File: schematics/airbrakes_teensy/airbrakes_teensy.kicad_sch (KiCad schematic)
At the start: 13 parts, among them SW1 SW_SCREW, SW2 SW_limit, SW3 SW_limit, U6 XL1509-3.3

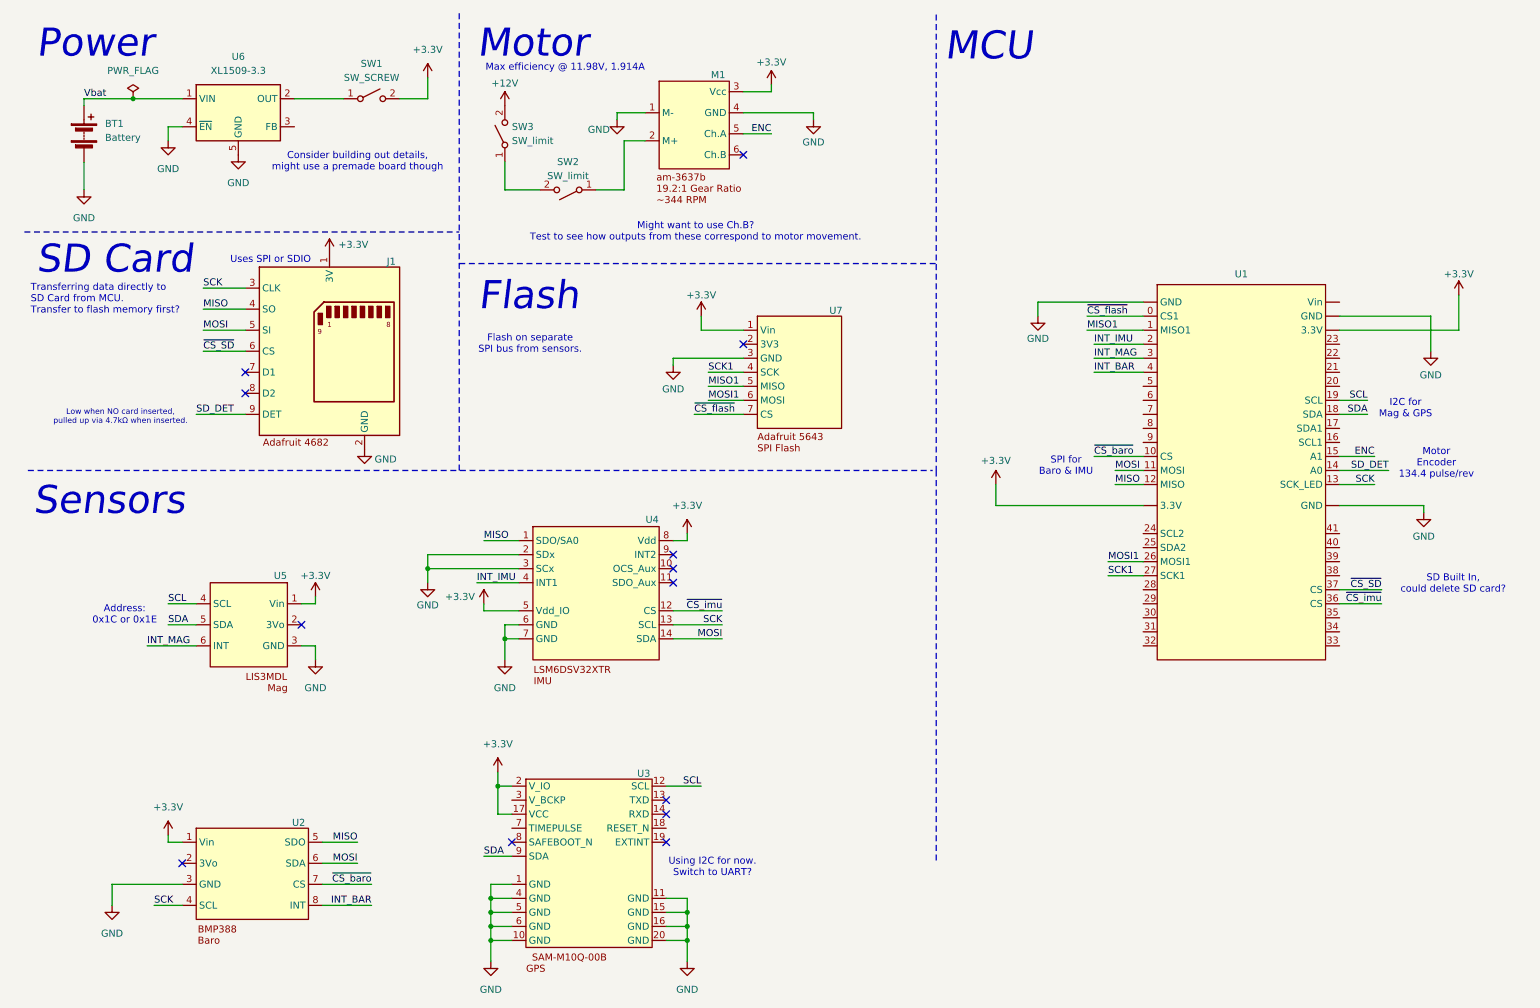
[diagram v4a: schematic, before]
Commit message: Add motor +12V power (3x lipos)
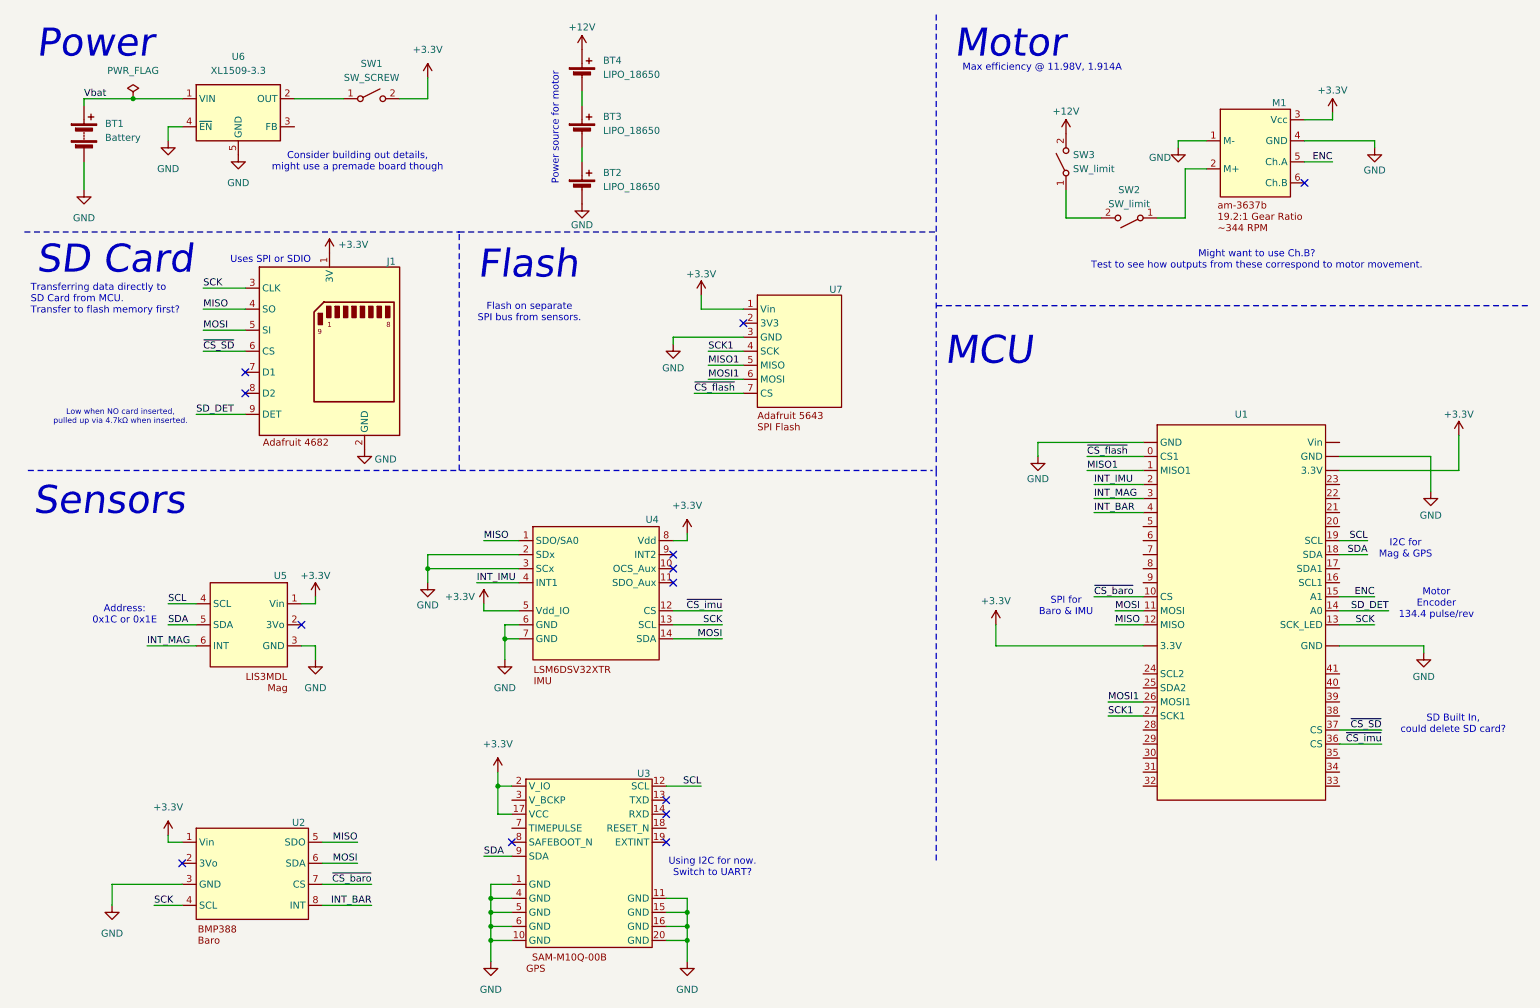
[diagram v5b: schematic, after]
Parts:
- added BT2, BT3, BT4: LIPO_18650, symbol Device:Battery_Cell
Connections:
- net +12V: now also BT4.1 (+)
- net GND: now also BT2.2 (-)
- new net: BT3.1 (+), BT4.2 (-)
- new net: BT2.1 (+), BT3.2 (-)
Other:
- note added: "Power source for motor"
- moved on the sheet: M1, SW2, SW3, U1, U7
